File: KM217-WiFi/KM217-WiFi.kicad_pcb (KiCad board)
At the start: 2 copper layers, 100.8 x 40 mm, 120 parts, among them J1 KM271-CON, J2 USB_B_Mini, J3 VSEL, J4 DEBUG, J5 ATS, J6 TSENS, J7 EXT, SW1 USER2, SW2 USER1, SW3 BOOT, SW4 RESET, U1 ESP32-WROOM-32E-N8, U2 AZ1117IH-3.3TRG1, U3 24LC1025, U4 SN74LV1T34DBV, U5 SN74LV1T34DBV, U6 PCA9306DC1, U7 DS2484

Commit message: feat: silkscreen labels, fiducials, gold finger fab note, v1.1.0
Main: EXT (J7) pinout labels, repo URL, hidden JLC order-number
placeholder under J7, J1 fab note (gold fingers yes, bevel not
possible), GOLD_FINGERS rule area, 3+3 fiducials. ETH: 3 bottom
fiducials (no room on top without moving parts). Revision v1.1.0.
DRC 0 errors on both boards.

Co-Authored-By: Claude Opus 5.5 <noreply@anthropic.com>
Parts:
- added FID1: Fiducial_1mm_Mask2mm, Fiducial_1mm_Mask2mm, F.Cu at (110.0, 111.0)
- added FID2: Fiducial_1mm_Mask2mm, Fiducial_1mm_Mask2mm, F.Cu at (116.0, 126.0)
- added FID3: Fiducial_1mm_Mask2mm, Fiducial_1mm_Mask2mm, F.Cu at (131.9, 121.0)
- added FID4: Fiducial_1mm_Mask2mm, Fiducial_1mm_Mask2mm, B.Cu at (81.0, 126.0)
- added FID5: Fiducial_1mm_Mask2mm, Fiducial_1mm_Mask2mm, B.Cu at (110.0, 111.0)
- added FID6: Fiducial_1mm_Mask2mm, Fiducial_1mm_Mask2mm, B.Cu at (157.9, 113.0)
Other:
- board text added: "3V3"
- board text added: "5V"
- board text added: "CS"
- board text added: "EXT"
- board text added: "FAB NOTE J1 (KM271 card edge): 12 gold fingers F+B, 1.6 mm FR4 (+-10%). Order option: Gold Fingers = YES (ENIG / hard gold on fingers), mask open over fingers. Bevel: NOT POSSIBLE - finger edge (y=124.25) is recessed 5.75 mm between the board legs (y=130) and JLC chamfers only boards >= 50x50 mm. Original module is used unbevelled. Fingers end 0.2 mm before the board edge; no vias/pads within 1 m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"
- board text added: "INT"
- board text added: "JLCJLCJLCJLC"
- board text added: "MISO"
- board text added: "MOSI"
- board text added: "SCK"
- board text added: "SCL"
- board text added: "SDA"
- board text added: "github.com/the78mole/km271-wifi"

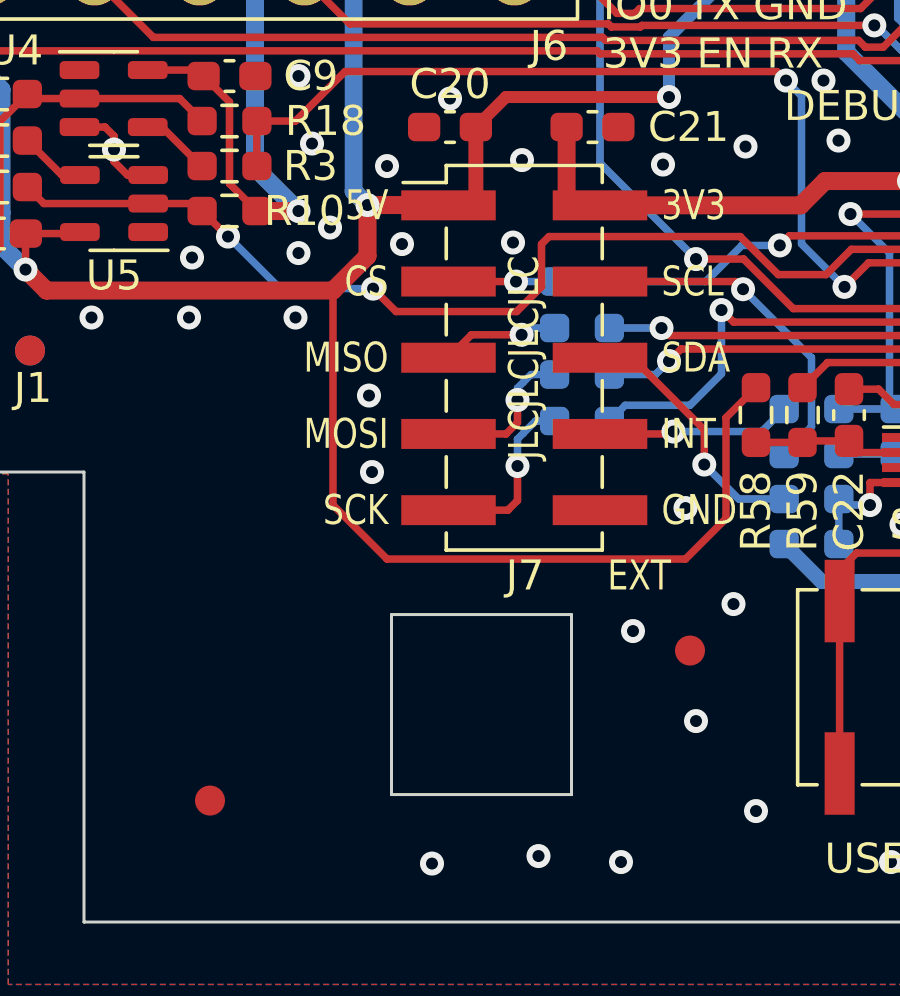
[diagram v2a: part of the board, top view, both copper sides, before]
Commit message: docs: JLCPCB production files, ordering guide and README section
Fab zips, BOM/CPL, iBOM, schematic/PCB PDFs, STEP and renders for both
boards (scripts/jlc/make_outputs.sh). DOC/JLCPCB-ordering.md: order
options, datasheet-checked part swaps, JLC compliance checklist, CPL
rotation verification, cost estimate. Before renders in IMG/jlc.

Co-Authored-By: Claude Opus 5.5 <noreply@anthropic.com>
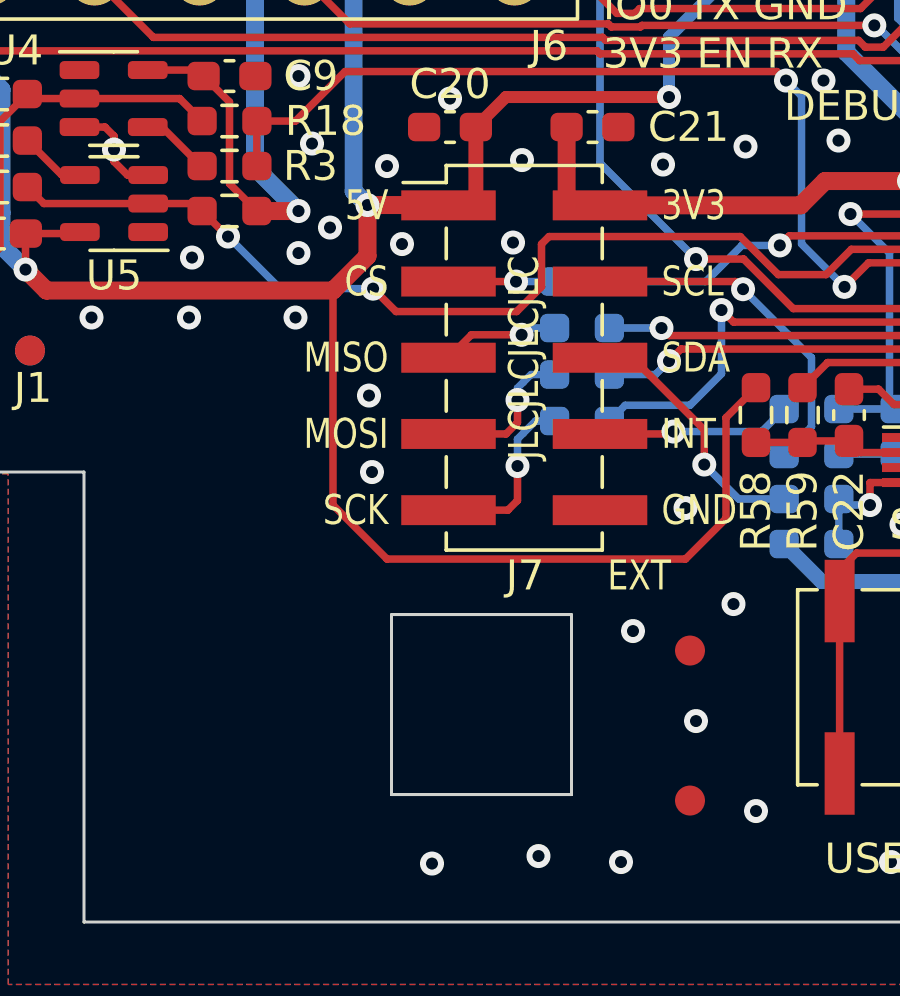
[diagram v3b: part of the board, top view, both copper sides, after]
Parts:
- moved FID2 16.8 mm to (131.9, 121.0)
- moved FID3 5.00 mm to (131.9, 126.0)
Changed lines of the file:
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@@
 			(at -2.5 0 0)
 			(layer "F.SilkS")
+			(hide yes)
 			(effects
 				(font
@@
 				(font
 					(size 1.27 1.27)
+					(thickness 0.15)
 				)
 			)
@@
 	(footprint "Fiducial_1mm_Mask2mm"
 		(layer "F.Cu")
-		(at 115.95 125.95)
+		(at 131.95 120.95)
 		(descr "Fiducial, circular marking, 1mm bare copper, 2mm soldermask opening (Level A)")
 		(tags "fiducial")
@@
 				(font
 					(size 1.27 1.27)
+					(thickness 0.15)
 				)
 			)
@@
 				(font
 					(size 1.27 1.27)
+					(thickness 0.15)
 				)
 			)
@@
 				(font
 					(size 1.27 1.27)
+					(thickness 0.15)
 				)
 			)
@@
 				(font
 					(size 1.27 1.27)
+					(thickness 0.15)
 				)
 			)
@@
 				(font
 					(size 1.27 1.27)
+					(thickness 0.15)
 				)
 			)
@@
 	(footprint "Fiducial_1mm_Mask2mm"
 		(layer "F.Cu")
-		(at 131.95 120.95)
+		(at 131.95 125.95)
 		(descr "Fiducial, circular marking, 1mm bare copper, 2mm soldermask opening (Level A)")
 		(tags "fiducial")
@@
 				(font
 					(size 1.27 1.27)
+					(thickness 0.15)
 				)
 			)
@@
 				(font
 					(size 1.27 1.27)
+					(thickness 0.15)
 				)
 			)

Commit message: feat(main): USB-C power input, 3D models for all parts, DRC/ERC warning cleanup
- J2 Mini-B -> HRO TYPE-C-31-M-12 (C165948), power only (D+/D- were
  unused): CC1/CC2 each 5k1 to GND (R69/R70, C23186), shield via R60
  as before. Local re-route around J2 only (scripts/jlc/usbc_swap.py),
  GND vias removed from under the metal shell. CPL offset verified
  against JLC footprint.
- 3D models in 3dmodels/ (project-relative): USB-C and TR1 from
  EasyEDA, stock B3SL/SOIC-8 for SW1-4/U3, approximate boxes for
  RJ45, WR-MM and WAGO (vendor models not available offline).
- Parity cleanup: power symbols instead of local GND/VBUS labels,
  PWR_FLAGs, SW1-4 footprint field, J8 not on board, fiducials
  board-only, field sync via netlist (includes excluded-from-BOM parts),
  ETH C25/C33 refdes, FID5 nudged. DRC 0 errors / 0 unconnected,
  ERC 0 errors on both boards.

Co-Authored-By: Claude Opus 5.5 <noreply@anthropic.com>
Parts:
- added R69: 5K1, Resistor_SMD:R_0603_1608Metric_Pad0.98x0.95mm_HandSolder, F.Cu at (79.5, 100.4)
- added R70: 5K1, Resistor_SMD:R_0603_1608Metric_Pad0.98x0.95mm_HandSolder, F.Cu at (77.0, 100.4)
- J2: value USB_B_Mini -> USB_C; footprint the78mole:USB_Mini-B_Wuerth_65100516121_Horizontal -> Connector_USB:USB_C_Receptacle_HRO_TYPE-C-31-M-12
- moved J2 2.75 mm to (78.3, 93.3)
- moved FID5 1.41 mm to (111.0, 112.0)
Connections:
- R60 pad 1: Net-(J2-Shield) -> /USB_SHIELD
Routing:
- net /USB_SHIELD: track 0.00 -> 23.3 mm
- net Net-(J2-Shield): track 23.0 -> 0.00 mm
- net VBUS: track 12.0 -> 21.3 mm, vias 1 -> 2
- net GND: track 25.7 -> 32.4 mm
- net Net-(J2-CC2): track 0.00 -> 2.30 mm
- net Net-(J2-CC1): track 0.00 -> 2.09 mm

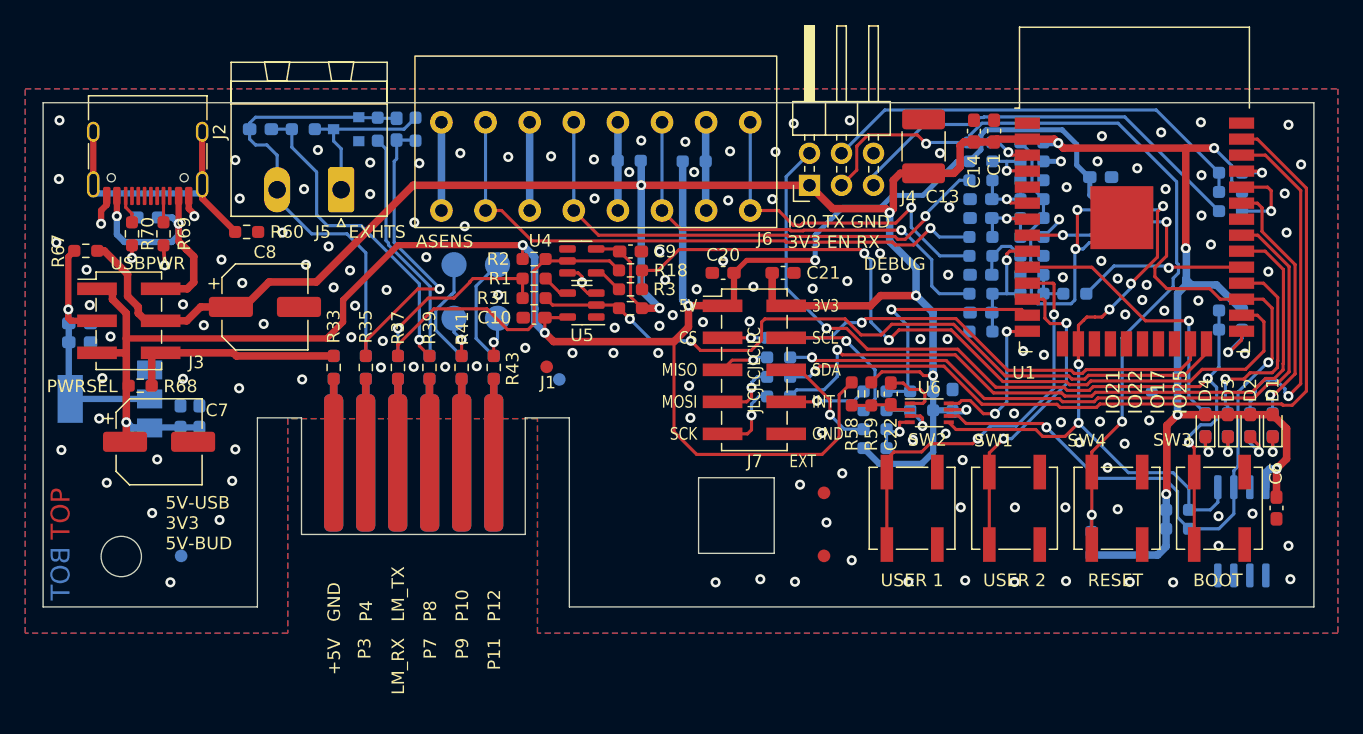
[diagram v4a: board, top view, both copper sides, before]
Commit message: fix: LED silkscreen order, visible refdes, fab notes, pour pullback
- Main: LED labels were reversed vs. nets (D1=IO21 ... D4=IO25); fixed.
- All refdes visible (R10, H1, ETH JP1-3 placed instead of hidden).
- ETH fiducials restored/placed clear of JP1 text and copper.
- Fab notes (stackup, finish, gold finger, assembly) on Cmts.User.
- Copper pours pulled back 0.5 mm from routed edges (zone-only rule).
- scripts/jlc/verify.py: pin-level netlist diff vs upstream, placement
  diff, BOM/CPL/PCB refdes consistency, hidden refdes, connector nets.

Co-Authored-By: Claude Opus 5.5 <noreply@anthropic.com>
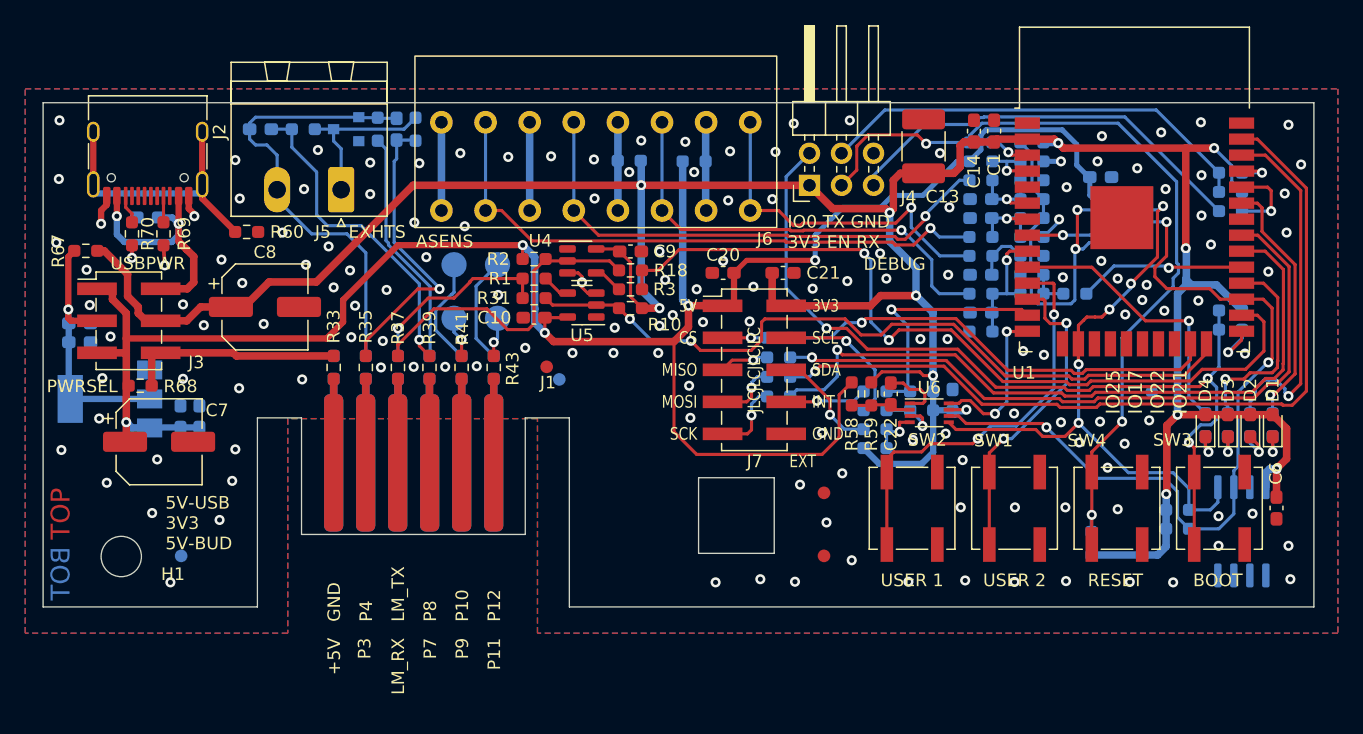
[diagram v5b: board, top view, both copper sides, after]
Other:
- board text added: "FAB NOTES ${TITLE} rev ${REVISION} Stackup: 2 layers, FR4 TG135, 1.6 mm +-10 pct, outer copper 1 oz (35 um) L1 F.Cu signal/GND pour | core 1.5 mm | L2 B.Cu signal/GND pour Finish: ENIG (gold fingers). Gold fingers: YES, bevel: NO (see J1 note) Mask green, silk white, vias tented. Min track/space 0.20/0.20 mm, min via 0.3/0.6 mm Assembly: Standard PCBA, both sides. BOM/CPL: production/bom.csv, pro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"
- board text added: "IO25 IO17 IO22 IO21"
- board text removed: "IO21 IO22 IO17 IO25"
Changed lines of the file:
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@@
 		(tags "resistor handsolder")
 		(property "Reference" "R10"
-			(at -2.5 0 0)
+			(at -2.7 -1.3 0)
 			(layer "F.SilkS")
-			(hide yes)
 			(effects
 				(font
@@
 		(tags "mounting hole 3.2mm no annular m3 din965")
 		(property "Reference" "H1"
-			(at 0 -3.8 0)
+			(at 4.1 1.4 0)
 			(layer "F.SilkS")
-			(hide yes)
 			(effects
 				(font
@@
 		)
 	)
-	(gr_text "IO21\nIO22\nIO17\nIO25"
+	(gr_text "IO25\nIO17\nIO22\nIO21"
 		(at 157.55 112.95 90)
 		(layer "F.SilkS")
@@
 		)
 	)
+	(gr_text "FAB NOTES ${TITLE} rev ${REVISION}\nStackup: 2 layers, FR4 TG135, 1.6 mm +-10 pct, outer copper 1 oz (35 um)\nL1 F.Cu signal/GND pour | core 1.5 mm | L2 B.Cu signal/GND pour\nFinish: ENIG (gold fingers). Gold fingers: YES, bevel: NO (see J1 note)\nMask green, silk white, vias tented. Min track/space 0.20/0.20 mm, min via 0.3/0.6 mm\nAssembly: Standard PCBA, both sides. BOM/CPL: production/bom.csv, production/positions.csv"
+		(at 69.95 140.05 0)
+		(layer "Cmts.User")
+		(effects
+			(font
+				(size 0.8 0.8)
+				(thickness 0.12)
+			)
+			(justify left)
+		)
+	)
